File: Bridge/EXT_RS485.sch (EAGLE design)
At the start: 8 parts, among them IC1 SN65HVD72D, X1 V1, X2 GND, X3 V2

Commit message: Minor Changes
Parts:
- added R1, R3: 10k, RCL:R0603
- added R2: 120R, RCL:R0603
- added X4, X5: TERM, Conn:WIREPADT1.6/0.9
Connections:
- new net N$13: R2.1, X4.S
- net +3V3: now also R3.2
- net DE: now also R1.2
- net GND: now also R1.1
- net N$11: now also R2.2
- net N$12: now also X5.S
- net RX: now also R3.1
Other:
- moved on the sheet: BUS-1, BUS-2
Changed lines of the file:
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@@
 <part name="X2" library="Conn" deviceset="WIREPAD" device="T1.6/0.9" value="GND"/>
 <part name="X3" library="Conn" deviceset="WIREPAD" device="T1.6/0.9" value="V2"/>
+<part name="R1" library="RCL" deviceset="R" device="0603" value="10k"/>
+<part name="GND4" library="supply1" deviceset="GND" device=""/>
+<part name="R2" library="RCL" deviceset="R" device="0603" value="120R"/>
+<part name="X4" library="Conn" deviceset="WIREPAD" device="T1.6/0.9" value="TERM"/>
+<part name="X5" library="Conn" deviceset="WIREPAD" device="T1.6/0.9" value="TERM"/>
+<part name="R3" library="RCL" deviceset="R" device="0603" value="10k"/>
+<part name="+3V3" library="supply1" deviceset="+3V3" device=""/>
 </parts>
 <sheets>
@@
 <instance part="C1" gate="1" x="193.04" y="71.12" rot="R270"/>
 <instance part="GND3" gate="1" x="200.66" y="71.12" rot="R90"/>
-<instance part="BUS" gate="-1" x="198.12" y="63.5"/>
-<instance part="BUS" gate="-2" x="198.12" y="58.42"/>
+<instance part="BUS" gate="-1" x="203.2" y="63.5"/>
+<instance part="BUS" gate="-2" x="203.2" y="58.42"/>
 <instance part="BUS" gate="-3" x="40.64" y="144.78" rot="R90"/>
 <instance part="BUS" gate="-4" x="55.88" y="81.28"/>
@@
 <instance part="X2" gate="1" x="43.18" y="81.28"/>
 <instance part="X3" gate="1" x="40.64" y="137.16" rot="R90"/>
+<instance part="R1" gate="G$1" x="154.94" y="45.72" rot="R90"/>
+<instance part="GND4" gate="1" x="154.94" y="38.1"/>
+<instance part="R2" gate="G$1" x="190.5" y="50.8" rot="R90"/>
+<instance part="X4" gate="1" x="190.5" y="43.18" rot="R90"/>
+<instance part="X5" gate="1" x="195.58" y="43.18" rot="R90"/>
+<instance part="R3" gate="G$1" x="154.94" y="76.2" rot="R90"/>
+<instance part="+3V3" gate="G$1" x="154.94" y="86.36"/>
 </instances>
 <busses>
@@
 <wire x1="198.12" y1="71.12" x2="195.58" y2="71.12" width="0.1524" layer="91"/>
 </segment>
+<segment>
+<pinref part="R1" gate="G$1" pin="1"/>
+<pinref part="GND4" gate="1" pin="GND"/>
+</segment>
 </net>
 <net name="SCL" class="0">
@@
 <pinref part="IC1" gate="G$1" pin="RO"/>
 <pinref part="IN" gate="-6" pin="S"/>
-<wire x1="147.32" y1="68.58" x2="157.48" y2="68.58" width="0.1524" layer="91"/>
+<wire x1="147.32" y1="68.58" x2="154.94" y2="68.58" width="0.1524" layer="91"/>
+<pinref part="R3" gate="G$1" pin="1"/>
+<wire x1="154.94" y1="68.58" x2="157.48" y2="68.58" width="0.1524" layer="91"/>
+<wire x1="154.94" y1="71.12" x2="154.94" y2="68.58" width="0.1524" layer="91"/>
+<junction x="154.94" y="68.58"/>
 </segment>
 </net>
@@
 <junction x="154.94" y="58.42"/>
 <pinref part="IN" gate="-4" pin="S"/>
+<pinref part="R1" gate="G$1" pin="2"/>
+<wire x1="154.94" y1="50.8" x2="154.94" y2="58.42" width="0.1524" layer="91"/>
 </segment>
 </net>
@@
 <junction x="185.42" y="71.12"/>
 </segment>
+<segment>
+<pinref part="R3" gate="G$1" pin="2"/>
+<pinref part="+3V3" gate="G$1" pin="+3V3"/>
+<wire x1="154.94" y1="83.82" x2="154.94" y2="81.28" width="0.1524" layer="91"/>
+</segment>
 </net>
 <net name="N$11" class="0">
@@
 <pinref part="IC1" gate="G$1" pin="B"/>
 <pinref part="BUS" gate="-1" pin="K"/>
-<wire x1="195.58" y1="63.5" x2="182.88" y2="63.5" width="0.1524" layer="91"/>
+<wire x1="200.66" y1="63.5" x2="190.5" y2="63.5" width="0.1524" layer="91"/>
+<pinref part="R2" gate="G$1" pin="2"/>
+<wire x1="190.5" y1="63.5" x2="182.88" y2="63.5" width="0.1524" layer="91"/>
+<wire x1="190.5" y1="55.88" x2="190.5" y2="63.5" width="0.1524" layer="91"/>
+<junction x="190.5" y="63.5"/>
 </segment>
 </net>
@@
 <pinref part="IC1" gate="G$1" pin="A"/>
 <pinref part="BUS" gate="-2" pin="K"/>
+<wire x1="200.66" y1="58.42" x2="195.58" y2="58.42" width="0.1524" layer="91"/>
+<pinref part="X5" gate="1" pin="S"/>
 <wire x1="195.58" y1="58.42" x2="182.88" y2="58.42" width="0.1524" layer="91"/>
+<wire x1="195.58" y1="45.72" x2="195.58" y2="58.42" width="0.1524" layer="91"/>
+<junction x="195.58" y="58.42"/>
 </segment>
 </net>
@@
 </segment>
 </net>
+<net name="N$13" class="0">
+<segment>
+<pinref part="R2" gate="G$1" pin="1"/>
+<pinref part="X4" gate="1" pin="S"/>
+</segment>
+</net>

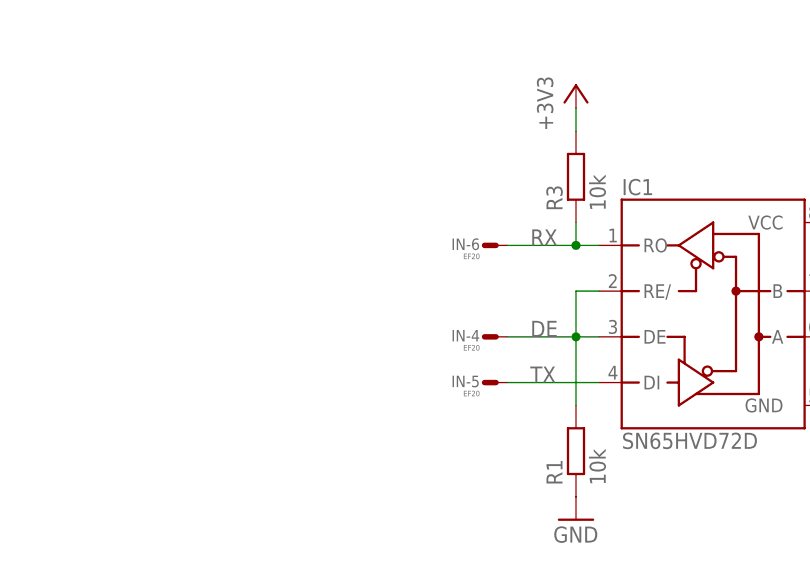
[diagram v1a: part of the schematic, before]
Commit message: Added LED's
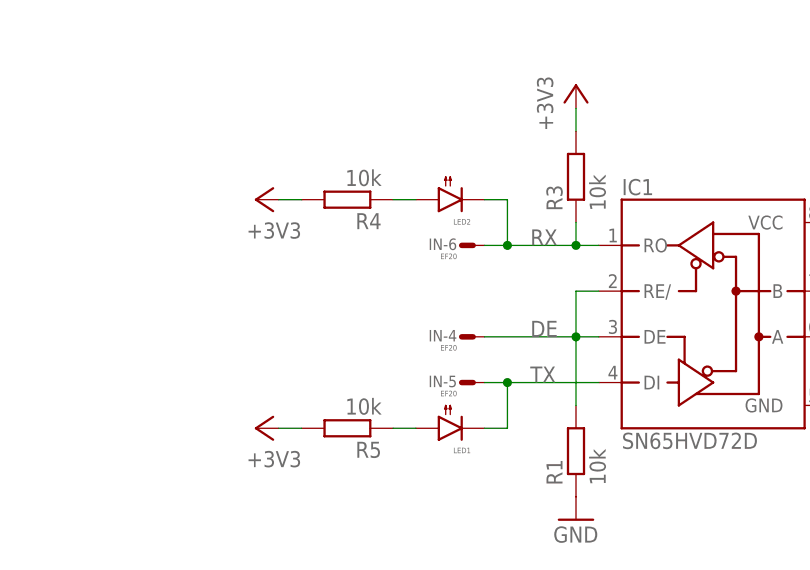
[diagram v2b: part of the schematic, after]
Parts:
- added LED1, LED2: (no value), Optic:LED0805
- added R4, R5: 10k, RCL:R0603
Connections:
- new net N$14: LED2.A, R4.1
- new net N$15: LED1.A, R5.1
- net +3V3: now also R4.2, R5.2
- net RX: now also LED2.C
- net TX: now also LED1.C
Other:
- moved on the sheet: IN-4, IN-5, IN-6
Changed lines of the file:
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@@
 <part name="R3" library="RCL" deviceset="R" device="0603" value="10k"/>
 <part name="+3V3" library="supply1" deviceset="+3V3" device=""/>
+<part name="LED1" library="Optic" deviceset="LED" device="0805"/>
+<part name="LED2" library="Optic" deviceset="LED" device="0805"/>
+<part name="R4" library="RCL" deviceset="R" device="0603" value="10k"/>
+<part name="R5" library="RCL" deviceset="R" device="0603" value="10k"/>
+<part name="+3V4" library="supply1" deviceset="+3V3" device=""/>
+<part name="+3V5" library="supply1" deviceset="+3V3" device=""/>
 </parts>
 <sheets>
@@
 <instance part="IN" gate="-1" x="35.56" y="121.92" rot="MR180"/>
 <instance part="IN" gate="-2" x="35.56" y="88.9" rot="MR180"/>
-<instance part="IN" gate="-4" x="144.78" y="58.42" rot="MR180"/>
-<instance part="IN" gate="-5" x="144.78" y="53.34" rot="MR180"/>
-<instance part="IN" gate="-6" x="144.78" y="68.58" rot="MR180"/>
+<instance part="IN" gate="-4" x="142.24" y="58.42" rot="MR180"/>
+<instance part="IN" gate="-5" x="142.24" y="53.34" rot="MR180"/>
+<instance part="IN" gate="-6" x="142.24" y="68.58" rot="MR180"/>
 <instance part="IN" gate="-7" x="35.56" y="119.38" rot="MR180"/>
 <instance part="IN" gate="-8" x="35.56" y="116.84" rot="MR180"/>
@@
 <instance part="R3" gate="G$1" x="154.94" y="76.2" rot="R90"/>
 <instance part="+3V3" gate="G$1" x="154.94" y="86.36"/>
+<instance part="LED1" gate="1" x="139.7" y="48.26" rot="R90"/>
+<instance part="LED2" gate="1" x="139.7" y="73.66" rot="R90"/>
+<instance part="R4" gate="G$1" x="129.54" y="73.66" rot="R180"/>
+<instance part="R5" gate="G$1" x="129.54" y="48.26" rot="R180"/>
+<instance part="+3V4" gate="G$1" x="119.38" y="73.66" rot="R90"/>
+<instance part="+3V5" gate="G$1" x="119.38" y="48.26" rot="R90"/>
 </instances>
 <busses>
@@
 <pinref part="IC1" gate="G$1" pin="RO"/>
 <pinref part="IN" gate="-6" pin="S"/>
+<wire x1="144.78" y1="68.58" x2="147.32" y2="68.58" width="0.1524" layer="91"/>
+<pinref part="R3" gate="G$1" pin="1"/>
 <wire x1="147.32" y1="68.58" x2="154.94" y2="68.58" width="0.1524" layer="91"/>
-<pinref part="R3" gate="G$1" pin="1"/>
 <wire x1="154.94" y1="68.58" x2="157.48" y2="68.58" width="0.1524" layer="91"/>
 <wire x1="154.94" y1="71.12" x2="154.94" y2="68.58" width="0.1524" layer="91"/>
 <junction x="154.94" y="68.58"/>
+<pinref part="LED2" gate="1" pin="C"/>
+<wire x1="144.78" y1="73.66" x2="147.32" y2="73.66" width="0.1524" layer="91"/>
+<wire x1="147.32" y1="73.66" x2="147.32" y2="68.58" width="0.1524" layer="91"/>
+<junction x="147.32" y="68.58"/>
 </segment>
 </net>
@@
 <pinref part="IC1" gate="G$1" pin="DI"/>
 <pinref part="IN" gate="-5" pin="S"/>
+<wire x1="144.78" y1="53.34" x2="147.32" y2="53.34" width="0.1524" layer="91"/>
+<pinref part="LED1" gate="1" pin="C"/>
 <wire x1="147.32" y1="53.34" x2="157.48" y2="53.34" width="0.1524" layer="91"/>
+<wire x1="144.78" y1="48.26" x2="147.32" y2="48.26" width="0.1524" layer="91"/>
+<wire x1="147.32" y1="48.26" x2="147.32" y2="53.34" width="0.1524" layer="91"/>
+<junction x="147.32" y="53.34"/>
 </segment>
 </net>
@@
 <segment>
 <label x="149.86" y="58.42" size="1.778" layer="95"/>
-<wire x1="147.32" y1="58.42" x2="154.94" y2="58.42" width="0.1524" layer="91"/>
+<wire x1="144.78" y1="58.42" x2="154.94" y2="58.42" width="0.1524" layer="91"/>
 <wire x1="154.94" y1="58.42" x2="157.48" y2="58.42" width="0.1524" layer="91"/>
 <wire x1="154.94" y1="58.42" x2="154.94" y2="63.5" width="0.1524" layer="91"/>
@@
 <wire x1="154.94" y1="83.82" x2="154.94" y2="81.28" width="0.1524" layer="91"/>
 </segment>
+<segment>
+<pinref part="+3V4" gate="G$1" pin="+3V3"/>
+<pinref part="R4" gate="G$1" pin="2"/>
+<wire x1="121.92" y1="73.66" x2="124.46" y2="73.66" width="0.1524" layer="91"/>
+</segment>
+<segment>
+<pinref part="+3V5" gate="G$1" pin="+3V3"/>
+<pinref part="R5" gate="G$1" pin="2"/>
+<wire x1="121.92" y1="48.26" x2="124.46" y2="48.26" width="0.1524" layer="91"/>
+</segment>
 </net>
 <net name="N$11" class="0">
@@
 </segment>
 </net>
+<net name="N$14" class="0">
+<segment>
+<pinref part="LED2" gate="1" pin="A"/>
+<pinref part="R4" gate="G$1" pin="1"/>
+<wire x1="137.16" y1="73.66" x2="134.62" y2="73.66" width="0.1524" layer="91"/>
+</segment>
+</net>
+<net name="N$15" class="0">
+<segment>
+<pinref part="LED1" gate="1" pin="A"/>
+<pinref part="R5" gate="G$1" pin="1"/>
+<wire x1="137.16" y1="48.26" x2="134.62" y2="48.26" width="0.1524" layer="91"/>
+</segment>
+</net>

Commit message: Added S4M13
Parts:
- removed BUS: BUS, Conn:1725672
- removed LED1, LED2: (no value), Optic:LED0805
- removed R4, R5: 10k, RCL:R0603
- removed X1: V1, Conn:WIREPADT1.6/0.9
- removed X2: GND, Conn:WIREPADT1.6/0.9
- removed X3: V2, Conn:WIREPADT1.6/0.9
- added C2: nc, RCL:C1206
- added CN1, CN2: RJ11, Conn:CON6RJ11V
- added D1: PMEG4005, Diode:D-SCHOTKY323
- added IC2: TSR 0.5-2450, DCDC:78XXS3
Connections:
- net N$13 renamed BUS-R
- removed net N$12: BUS-2.K, IC1.A, X5.S
- removed net N$14: LED2.A, R4.1
- removed net N$15: LED1.A, R5.1
- new net BUS-A: CN1-3.S, CN2-3.S, IC1.A, X5.S
- new net BUS-B: CN1-2.S, CN2-2.S, IC1.B, R2.2
- new net VOUT: IC2.OUT, IN-1.S
- net +3V3: no longer R4.2, R5.2
- net GND: now also C2.1, CN1-5.S, CN2-5.S, IC2.GND; no longer BUS-4.K, X2.S
- net N$11: now also C2.2, D1.C, IC2.IN; no longer BUS-1.K, IC1.B, R2.2
- net RX: no longer LED2.C
- net TX: no longer LED1.C
- net VIN: now also CN1-4.S, CN2-4.S, D1.A; no longer BUS-3.K, IN-1.S, X1.S, X3.S
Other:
- moved on the sheet: IN-1, OUT-1
